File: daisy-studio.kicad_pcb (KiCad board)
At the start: 4 copper layers, 270 x 65 mm, 101 parts, among them J1 Power, J10 Earth, J2 GPIO Header, J3 Micro_SD_Card, J4 NCJ6FA-H-0, J5 NCJ6FA-H-0, J6 Conn_01x04_Pin, J7 Earth, J8 NCJ6FA-H-0, J9 NCJ6FA-H-0, Q1 SI2301CDS-T1-GE3, U1 TMA-1212D, U2 TPS54302, U3 Daisy_Seed, U4 H11L1SM, U5 THAT1246, U6 THAT1246, U7 THAT1646, U8 THAT1646

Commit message: lots of pcb work
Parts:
- removed the C11 at (68.6, 119.5)
- removed the D5 at (132.2, 118.9)
- removed the H3 at (199.2, 112.3)
- removed the H3 at (59.6, 77.8)
- removed the J7 at (119.1, 82.4)
- removed J_DC1: Barrel_Jack_2.1mm, Connector_BarrelJack:BarrelJack_Horizontal
- removed J_IN_ST1, J_OUT_ST1: STX-3100-3CB, Connector_Audio:Jack_3.5mm_Kycon_STX-3100-3CB
- removed J_MIDI_IN_1, J_MIDI_OUT_1, J_MIDI_THRU1: SDS-50J, daisy-studio:SDS50J
- removed the R23 at (115.0, 117.3)
- removed S1: LC2255EESP, daisy-studio:LC2255EESP
- removed the U1 at (316.8, 108.5)
- added C28: 1n, Capacitor_SMD:C_0805_2012Metric, F.Cu at (115.0, 70.1)
- added C29: 1n, Capacitor_SMD:C_0805_2012Metric, F.Cu at (120.0, 65.4)
- added C30: 100n, Capacitor_SMD:C_0805_2012Metric, F.Cu at (153.6, 51.1)
- added C31: 100n, Capacitor_SMD:C_0805_2012Metric, F.Cu at (122.0, 65.4)
- added C32: 10u, Capacitor_SMD:C_0805_2012Metric, F.Cu at (140.4, 54.5)
- added C33: 10u, Capacitor_SMD:C_0805_2012Metric, F.Cu at (131.4, 59.9)
- added C34: 100n, Capacitor_SMD:C_0805_2012Metric, F.Cu at (142.4, 54.5)
- added C35: 100n, Capacitor_SMD:C_0805_2012Metric, F.Cu at (134.8, 59.9)
- added C36: 10u, Capacitor_SMD:C_0805_2012Metric, F.Cu at (122.8, 54.5)
- added C37: 10u, Capacitor_SMD:C_0805_2012Metric, F.Cu at (113.8, 59.9)
- added C38: 100n, Capacitor_SMD:C_0805_2012Metric, F.Cu at (124.8, 54.5)
- added C39: 100n, Capacitor_SMD:C_0805_2012Metric, F.Cu at (117.2, 59.9)
- added C40: 47u, Capacitor_SMD:C_1206_3216Metric, F.Cu at (156.3, 62.2)
- added C41: 47u, Capacitor_SMD:C_1206_3216Metric, F.Cu at (164.2, 59.8)
- added C42: 47u, Capacitor_SMD:C_1206_3216Metric, F.Cu at (156.3, 69.7)
- added C43: 47u, Capacitor_SMD:C_1206_3216Metric, F.Cu at (164.2, 67.5)
- added C9: 1n C0G, Capacitor_SMD:C_0603_1608Metric, F.Cu at (183.5, 63.4)
- added D13: SM4004, Diode_SMD:D_MELF, F.Cu at (61.5, 54.6)
- added D14: LED, LED_THT:LED_D3.0mm, F.Cu at (105.4, 112.9)
- added D15: LED, LED_THT:LED_D3.0mm, F.Cu at (131.4, 112.9)
- added D2: SMBJ15CA, Diode_SMD:D_SMB, F.Cu at (262.8, 78.1)
- added H10: MountingHole, MountingHole:MountingHole_3.2mm_M3, F.Cu at (90.2, 112.9)
- added H11: MountingHole, MountingHole:MountingHole_3.2mm_M3, F.Cu at (149.9, 112.9)
- added H3: MountingHole_Pad, MountingHole:MountingHole_3.2mm_M3_Pad_Via, F.Cu at (149.9, 30.4)
- added H6: MountingHole, MountingHole:MountingHole_3.2mm_M3, F.Cu at (79.6, 96.0)
- added H7: MountingHole, MountingHole:MountingHole_3.2mm_M3, F.Cu at (259.2, 97.8)
- added H8: MountingHole, MountingHole:MountingHole_3.2mm_M3, F.Cu at (256.5, 30.4)
- added H9: MountingHole, MountingHole:MountingHole_3.2mm_M3, F.Cu at (30.4, 112.9)
- added J13: Conn_02x10_Odd_Even, Connector_IDC:IDC-Header_2x10_P2.54mm_Vertical, F.Cu at (101.8, 55.9)
- added J14: Conn_02x10_Odd_Even, Connector_IDC:IDC-Header_2x10_P2.54mm_Vertical, F.Cu at (101.8, 138.4)
- added J2: Conn_02x04_Odd_Even, Connector_PinHeader_2.54mm:PinHeader_2x04_P2.54mm_Vertical, F.Cu at (158.3, 54.8)
- added J3: Conn_02x04_Odd_Even, Connector_PinHeader_2.54mm:PinHeader_2x04_P2.54mm_Vertical, F.Cu at (172.6, 52.6)
- added J5: SDS-50J, daisy-studio:SDS50J, F.Cu at (203.2, 37.9)
- added PS1: RS3-1212D, daisy-studio:TMR1210, F.Cu at (247.6, 86.5)
- added Q2: MMBT3904, Package_TO_SOT_SMD:SOT-23, F.Cu at (131.7, 65.8)
- added Q3: MMBT3904, Package_TO_SOT_SMD:SOT-23, F.Cu at (139.3, 69.3)
- added Q4: MMBT3906, Package_TO_SOT_SMD:SOT-23, F.Cu at (131.7, 69.3)
- added Q5: MMBT3906, Package_TO_SOT_SMD:SOT-23, F.Cu at (139.2, 65.8)
- added R19: 2k2 1%, Resistor_SMD:R_0805_2012Metric, F.Cu at (89.2, 72.1)
- added R27: 3.3k 1%, Resistor_SMD:R_0805_2012Metric, F.Cu at (123.7, 69.1)
- added R28: 3.3k 1%, Resistor_SMD:R_0805_2012Metric, F.Cu at (123.7, 71.0)
- added R29: 1k, Resistor_SMD:R_0805_2012Metric, F.Cu at (88.5, 50.3)
- added R30: 1k, Resistor_SMD:R_0805_2012Metric, F.Cu at (90.6, 50.3)
- added R31: 10k 1%, Resistor_SMD:R_0805_2012Metric, F.Cu at (158.6, 59.2)
- added R32: 1.5k 1%, Resistor_SMD:R_0805_2012Metric, F.Cu at (158.6, 62.9)
- added R33: 1.5k 1%, Resistor_SMD:R_0805_2012Metric, F.Cu at (166.6, 59.2)
- added R34: 10k 1%, Resistor_SMD:R_0805_2012Metric, F.Cu at (166.6, 62.7)
- added R35: 10k 1%, Resistor_SMD:R_0805_2012Metric, F.Cu at (158.6, 66.7)
- added R36: 1.5k 1%, Resistor_SMD:R_0805_2012Metric, F.Cu at (158.6, 70.3)
- added R37: 1.5k 1%, Resistor_SMD:R_0805_2012Metric, F.Cu at (166.6, 66.9)
- added R38: 10k 1%, Resistor_SMD:R_0805_2012Metric, F.Cu at (166.6, 70.4)
- added RV1: 10k, Potentiometer_THT:Potentiometer_Bourns_3296W_Vertical, F.Cu at (77.5, 65.0)
- added RV2: 10k, Potentiometer_THT:Potentiometer_Bourns_3296W_Vertical, F.Cu at (104.5, 65.1)
- added RV3: 10k, Potentiometer_THT:Potentiometer_Bourns_3296W_Vertical, F.Cu at (152.2, 68.9)
- added RV4: 10k, Potentiometer_THT:Potentiometer_Bourns_3296W_Vertical, F.Cu at (146.7, 68.9)
- added RV5: 10k log, Potentiometer_THT:Potentiometer_Alpha_RD901F-40-00D_Single_Vertical_CircularHoles, F.Cu at (104.2, 131.4)
- added RV6: 10k log, Potentiometer_THT:Potentiometer_Alpha_RD901F-40-00D_Single_Vertical_CircularHoles, F.Cu at (44.7, 131.4)
- added RV7: 10k log, Potentiometer_THT:Potentiometer_Alpha_RD901F-40-00D_Single_Vertical_CircularHoles, F.Cu at (130.2, 131.4)
- added RV8: 10k log, Potentiometer_THT:Potentiometer_Alpha_RD901F-40-00D_Single_Vertical_CircularHoles, F.Cu at (71.2, 131.4)
- added SW1: Power, Connector_JST:JST_VH_B2P-VH_1x02_P3.96mm_Vertical, F.Cu at (254.6, 39.1)
- added U10: THAT1246, Package_SO:SOIC-8_3.9x4.9mm_P1.27mm, F.Cu at (135.5, 56.0)
- added U4: OPA1656ID, Package_SO:SOIC-8_3.9x4.9mm_P1.27mm, F.Cu at (91.0, 67.5)
- added U5: THAT1646, Package_SO:SOIC-8_3.9x4.9mm_P1.27mm, F.Cu at (46.7, 64.7)
- C10: value 10u -> 1n C0G; footprint Capacitor_SMD:C_0805_2012Metric -> Capacitor_SMD:C_0603_1608Metric
- C12, C14, C26: value 10u -> 100n
- C13, C15: value 100n -> 1n
- C16, C17: value 10u -> 100p C0G
- C4: value 100u/25V -> 100u 25V
- C6, C7: value 22u -> 22u 25V; footprint Capacitor_SMD:C_0805_2012Metric -> Capacitor_SMD:C_1206_3216Metric
- C8: value 75pf -> 75pF
- D1: value SMBJ15A -> SMBJ15CA
- D10, D11, D12, D6, D7, D8, D9: footprint Diode_SMD:D_SMA -> Diode_SMD:D_MELF
- D3: value BAT54S -> SMBJ15CA; footprint Package_TO_SOT_SMD:SOT-23 -> Diode_SMD:D_SMB
- D4: value BAT54S -> SMAJ5.0A; footprint Package_TO_SOT_SMD:SOT-23 -> Diode_SMD:D_SMA
- D5: renamed from D2; value 1N4148W -> 1N4148WS; footprint Diode_SMD:D_SOD-123 -> Diode_SMD:D_SOD-323
- H1, H2: value MountingHole -> MountingHole_Pad; footprint MountingHole:MountingHole_3.2mm_M3 -> MountingHole:MountingHole_3.2mm_M3_Pad_Via
- J1: value Power -> Barrel_Jack_MountingPin; footprint Connector_PinHeader_2.54mm:PinHeader_2x04_P2.54mm_Vertical -> Connector_BarrelJack:BarrelJack_Horizontal
- J10: value Earth -> NCJ6FA-H-0; footprint MountingHole:MountingHole_3.2mm_M3_Pad_Via -> Connector_Audio:Jack_XLR-6.35mm_Neutrik_NCJ6FA-H-0_Horizontal
- J6: value Conn_01x04_Pin -> SDS-50J; footprint Connector_PinHeader_2.54mm:PinHeader_1x04_P2.54mm_Vertical -> daisy-studio:SDS50J
- J7: renamed from J2; value GPIO Header -> Conn_02x12_Odd_Even
- J8: value NCJ6FA-H-0 -> SDS-50J; footprint Connector_Audio:Jack_XLR-6.35mm_Neutrik_NCJ6FA-H-0_Horizontal -> daisy-studio:SDS50J
- JP1: value Earth-Gnd Disconnect -> SolderJumper_2_Bridged
- Q1: footprint Package_TO_SOT_SMD:SOT-23 -> daisy-studio:SOT95P237X112-3N
- R10, R11, R7, R8, R9: value 47K -> 47k
- R20: value 1.2k -> 2k2 1%; footprint Resistor_SMD:R_0603_1608Metric -> Resistor_SMD:R_0805_2012Metric
- R21, R22: value 100k -> 15k; footprint Resistor_SMD:R_0603_1608Metric -> Resistor_SMD:R_0805_2012Metric
- R23: renamed from R19; value 1.2k -> 10k; footprint Resistor_SMD:R_0603_1608Metric -> Resistor_SMD:R_0805_2012Metric
- R24: value 100k -> 10k; footprint Resistor_SMD:R_0603_1608Metric -> Resistor_SMD:R_0805_2012Metric
- R25, R26: value 120R -> 12k 1%; footprint Resistor_SMD:R_0603_1608Metric -> Resistor_SMD:R_0805_2012Metric
- R3: value 13.7k -> 13.7k 1%
- R4: value 49.9R -> 49.9R 1%
- R6: value 13.3k 1% -> 13.3K 1%
- U2: renamed from U3; footprint daisy-studio:DAISY_SEED_SMT -> daisy-studio:DAISY_SEED
- U3: renamed from U4; value H11L1SM -> H11L1
- U6: value THAT1246 -> THAT1646
- U7: value THAT1646 -> OPA1656ID
- U8: value THAT1646 -> LM2903
- moved H5 288.4 mm to (31.1, 97.6)
- moved D3 186.5 mm to (261.8, 70.1), turned to 0 degrees
- moved D4 150.0 mm to (253.2, 69.0), turned to 0 degrees
- moved H4 139.8 mm to (185.3, 96.9)
- moved C21 131.0 mm to (46.9, 69.1), turned to 0 degrees
- moved C10 128.7 mm to (183.5, 66.0), turned to 0 degrees
- moved J9 126.5 mm to (40.2, 44.0)
- moved C20 125.8 mm to (50.2, 69.1), turned to 0 degrees
- moved C25 125.8 mm to (64.8, 69.1), turned to 0 degrees
- moved C24 124.6 mm to (68.3, 69.1), turned to 0 degrees
- moved D10 118.3 mm to (43.4, 58.1)
- moved C23 117.0 mm to (69.8, 63.0), turned to -90 degrees
- moved J1 114.9 mm to (246.8, 39.0)
- moved D6 113.9 mm to (50.5, 58.1), turned to 0 degrees
- moved D11 113.7 mm to (43.4, 54.6), turned to 0 degrees
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- renumbered C9 to C11, J4 to J11, J5 to J12, J3 to J4, U2 to U1, U5 to U9
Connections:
- C10 pad 1: +12VA -> AUDIO_IN_L
- C12 pad 1: GND -> -12VA
- C12 pad 2: -12VA -> GND
- C13 pad 1: GND -> -12VA
- C13 pad 2: -12VA -> GND
- C16 pad 1: GND -> Net-(U4A--)
- C16 pad 2: -12VA -> OUT_OPA_L
- C17 pad 1: Net-(S1-NO_1) -> Net-(U4B--)
- C17 pad 2: AUDIO_IN_L -> OUT_OPA_R
- C18 pad 1: Net-(S1-NO_2) -> +12VA
- C18 pad 2: AUDIO_IN_R -> GND
- C19 pad 2: -12VA -> +12VA
- C20 pad 1: +12VA -> -12VA
- C21 pad 1: +12VA -> GND
- C21 pad 2: GND -> -12VA
- C22 pad 1: GND -> +12VA
- C22 pad 2: -12VA -> GND
- C23 pad 2: -12VA -> +12VA
- C24 pad 1: +12VA -> -12VA
- C25 pad 1: +12VA -> GND
- C25 pad 2: GND -> -12VA
- C26 pad 1: GND -> -12VA
- C26 pad 2: -12VA -> GND
- C27 pad 1: GND -> -12VA
- C27 pad 2: -12VA -> GND
- D1 pad 2: GND -> Net-(D1-A2)
- D10 pad 1: Net-(D10-K) -> +12VA
- D10 pad 2: -12VA -> Net-(D10-A)
- D11 pad 1: Net-(D11-K) -> Net-(D10-A)
- D12 pad 1: Net-(D12-K) -> +12VA
- D12 pad 2: -12VA -> Net-(D12-A)
- D3 pad 1: GND -> +12VA
- D3 pad 2: +5V -> GND
- D4 pad 1: GND -> +5V
- D4 pad 2: +5V -> GND
- D6 pad 2: Net-(D10-K) -> Net-(D6-A)
- D7 pad 1: +12VA -> Net-(D6-A)
- D7 pad 2: Net-(D11-K) -> -12VA
- D8 pad 2: Net-(D12-K) -> Net-(D8-A)
- D9 pad 1: Net-(D5-A) (its old number) -> Net-(D8-A)
- J1 pad 1: +5V -> /Power/+12V_IN
- J1 pad 2: +12VA -> Net-(D1-A2)
- J1 pad 3: GND -> (no net)
- J10 pad 1: Earth -> CHASSIS
- J11 pad 1: Earth -> CHASSIS
- J11 pad G: Earth -> CHASSIS
- J11 pad S: Earth -> CHASSIS
- J12 pad 1: Earth -> CHASSIS
- J12 pad 2: Net-(U6-In+) -> Net-(U10A-+)
- J12 pad 3: Net-(U6-In-) -> Net-(U10A--)
- J12 pad G: Earth -> CHASSIS
- J12 pad R: Net-(U6-In-) -> Net-(U10A--)
- J12 pad S: Earth -> CHASSIS
- J12 pad T: Net-(U6-In+) -> Net-(U10A-+)
- J4 pad 10: GND -> (no net)
- J4 pad 11: GND -> (no net)
- J6 pad 1: AUDIO_IN_L -> unconnected-(J6-Pad1)
- J6 pad 2: AUDIO_IN_R -> GND
- J6 pad 3: AUDIO_OUT_L -> unconnected-(J6-Pad3)
- J6 pad 4: AUDIO_OUT_R -> Net-(J6-Pad4)
- J8 pad 1: Earth -> unconnected-(J8-Pad1)
- J8 pad 2: Net-(D5-A) (its old number) -> GND
- J8 pad 3: Net-(D11-K) -> unconnected-(J8-Pad3)
- J9 pad 1: Earth -> CHASSIS
- J9 pad 2: Net-(D10-K) -> Net-(D6-A)
- J9 pad 3: Net-(D12-K) -> Net-(D10-A)
- J9 pad G: Earth -> CHASSIS
- J9 pad R: Net-(D12-K) -> Net-(D10-A)
- J9 pad S: Earth -> CHASSIS
- J9 pad T: Net-(D10-K) -> Net-(D6-A)
- JP1 pad 2: Earth -> CHASSIS
- Q1 pad 2: /Power/+12V_IN -> Net-(Q1-S)
- R1 pad 2: GND -> Net-(D1-A2)
- R12 pad 2: Net-(J_MIDI_OUT_1-Pad4) -> Net-(J6-Pad4)
- R13 pad 1: Net-(J_MIDI_OUT_1-Pad5) -> Net-(J6-Pad5)
- R17 pad 2: Net-(J_MIDI_THRU1-Pad4) -> Net-(J8-Pad4)
- R18 pad 2: Net-(J_MIDI_THRU1-Pad5) -> Net-(J8-Pad5)
- R20 pad 1: Net-(J_IN_ST1-R) -> Net-(U4B--)
- R20 pad 2: Net-(S1-NO_2) -> AUDIO_OUT_R
- R21 pad 1: AUDIO_IN_L -> Net-(R21-Pad1)
- R21 pad 2: +5V -> Net-(U4A--)
- R22 pad 1: GND -> Net-(R22-Pad1)
- R22 pad 2: AUDIO_IN_L -> Net-(U4B--)
- R23 pad 1: Net-(J_IN_ST1-T) -> Net-(R23-Pad1)
- R23 pad 2: Net-(S1-NO_1) -> Net-(U7A--)
- R24 pad 1: GND -> Net-(R24-Pad1)
- R24 pad 2: AUDIO_IN_R -> Net-(U10A-S)
- R25 pad 1: Net-(S1-COM_2) -> Net-(U7A--)
- R25 pad 2: GND -> IN_OPA_L
- R26 pad 1: Net-(S1-COM_1) -> Net-(U10A-S)
- R26 pad 2: GND -> IN_OPA_R
- U6 pad 1: GND -> Net-(D12-A)
- U6 pad 2: Net-(U6-In-) -> Net-(D12-A)
- U6 pad 3: Net-(U6-In+) -> GND
- U6 pad 4: -12VA -> OUT_WIPER_R
- U6 pad 5: Net-(J_IN_ST1-R) -> -12VA
- U6 pad 6: Net-(J_IN_ST1-R) -> +12VA
- U6 pad 7: +12VA -> Net-(D8-A)
- U6 pad 8: unconnected-(U6-NC-Pad8) -> Net-(D8-A)
- U7 pad 1: Net-(D5-A) (its old number) -> IN_OPA_L
- U7 pad 2: unconnected-(U7-Sense--Pad2) -> Net-(U7A--)
- U7 pad 4: AUDIO_OUT_L -> -12VA
- U7 pad 5: -12VA -> GND
- U7 pad 6: +12VA -> Net-(U10A-S)
- U7 pad 7: unconnected-(U7-Sense+-Pad7) -> IN_OPA_R
- U7 pad 8: Net-(D11-K) -> +12VA
- U8 pad 1: Net-(D10-K) -> CLIP_LED_K_L
- U8 pad 2: unconnected-(U8-Sense--Pad2) -> AUDIO_IN_L
- U8 pad 3: GND -> /Audio Input/IN_THRESH_L
- U8 pad 4: AUDIO_OUT_R -> -12VA
- U8 pad 5: -12VA -> /Audio Input/IN_THRESH_R
- U8 pad 6: +12VA -> AUDIO_IN_R
- U8 pad 7: unconnected-(U8-Sense+-Pad7) -> CLIP_LED_K_R
- U8 pad 8: Net-(D12-K) -> +12VA
- U9 pad 5: Net-(J_IN_ST1-T) -> Net-(U7A--)
- U9 pad 6: Net-(J_IN_ST1-T) -> Net-(R23-Pad1)
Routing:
- net +12VA: track 429.8 -> 32.9 mm, vias 13 -> 1
- net -12VA: track 404.0 -> 30.6 mm, vias 12 -> 2
- net +5V: track 312.3 -> 0.00 mm, vias 8 -> 0
- net +3V3D: track 198.3 -> 0.00 mm, vias 6 -> 0
- net Net-(J_IN_ST1-T): track 162.6 -> 0.00 mm, vias 1 -> 0
- net AUDIO_IN_L: track 184.2 -> 34.3 mm
- net CLIP_LED_K_R: track 0.00 -> 146.1 mm, vias 0 -> 3
- net Net-(J_IN_ST1-R): track 143.5 -> 0.00 mm, vias 1 -> 0
- net Net-(S1-NO_1): track 126.1 -> 0.00 mm, vias 2 -> 0
- net Net-(S1-NO_2): track 122.8 -> 0.00 mm
- net OUT_WIPER_L: track 0.00 -> 107.2 mm, vias 0 -> 1
- net +3V3A: track 105.5 -> 0.00 mm, vias 1 -> 0
- net CLIP_LED_K_L: track 0.00 -> 104.3 mm, vias 0 -> 1
- net AUDIO_IN_R: track 145.2 -> 42.4 mm, vias 2 -> 0
- net GPIO_D15: track 101.8 -> 0.00 mm
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- added copper zone on B.Cu, net CHASSIS
- added copper zone on In1.Cu, net CHASSIS
- removed copper zone on B.Cu, net Earth
- removed copper zone on In1.Cu, net Earth
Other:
- board size 270 x 65 mm -> 236.7 x 119.3 mm

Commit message: lots of pcb work
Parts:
- J2: value Conn_02x04_Odd_Even -> ~; footprint Connector_PinHeader_2.54mm:PinHeader_2x04_P2.54mm_Vertical -> Connector_PinHeader_2.54mm:PinHeader_2x03_P2.54mm_Vertical
- J4: value Micro_SD_Card -> Micro_SD_Card_Det2; footprint Connector_Card:microSD_HC_Hirose_DM3AT-SF-PEJM5 -> Connector_Card:microSD_HC_Hirose_DM3BT-DSF-PEJS; moved to B.Cu
- J7: footprint Connector_PinHeader_2.54mm:PinHeader_2x12_P2.54mm_Vertical_SMD -> Connector_PinHeader_2.54mm:PinHeader_2x14_P2.54mm_Vertical_SMD
- U2: footprint daisy-studio:DAISY_SEED -> daisy-studio:DAISY_SEED_SMT
- U3: footprint Package_SO:SO-6_4.4x3.6mm_P1.27mm -> Package_DIP:SMDIP-6_W7.62mm
- moved J3 131.2 mm to (302.9, 68.2), turned to 180 degrees
- moved C1 62.5 mm to (302.1, 86.5)
- moved C2 62.5 mm to (302.1, 89.5)
- moved L1 62.5 mm to (306.3, 86.2)
- moved L2 62.5 mm to (302.8, 86.5)
- moved H7 58.0 mm to (312.8, 75.5)
- moved J1 56.3 mm to (303.1, 39.0)
- moved H8 55.3 mm to (311.8, 30.4)
- moved J7 53.8 mm to (231.2, 50.1), turned to 0 degrees
- moved PS1 50.5 mm to (297.2, 77.3)
- moved C4 49.3 mm to (305.5, 50.7)
- moved C5 49.3 mm to (287.9, 60.7)
- moved C6 49.3 mm to (294.5, 69.0)
- moved C7 49.3 mm to (294.5, 67.0)
- moved C8 49.3 mm to (293.7, 60.4)
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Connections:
- J2 pad 6: (no net) -> GND
- J4 pad 10: (no net) -> unconnected-(J4-DET_A-Pad10)
- J4 pad 11: (no net) -> GND
- J4 pad 9: GND -> unconnected-(J4-DET_B-Pad9)
- J7 pad 1: GPIO_D0 -> unconnected-(J7-Pin_1-Pad1)
- J7 pad 10: GPIO_D19 -> unconnected-(J7-Pin_10-Pad10)
- J7 pad 11: GPIO_D11 -> GPIO_D8
- J7 pad 12: GPIO_D20 -> unconnected-(J7-Pin_12-Pad12)
- J7 pad 13: GPIO_D12 -> GPIO_D7
- J7 pad 14: GPIO_D21 -> unconnected-(J7-Pin_14-Pad14)
- J7 pad 15: GPIO_D29 -> unconnected-(J7-Pin_15-Pad15)
- J7 pad 16: GPIO_D22 -> unconnected-(J7-Pin_16-Pad16)
- J7 pad 17: GPIO_D30 -> unconnected-(J7-Pin_17-Pad17)
- J7 pad 18: GPIO_D23 -> unconnected-(J7-Pin_18-Pad18)
- J7 pad 19: GPIO_D28 -> unconnected-(J7-Pin_19-Pad19)
- J7 pad 2: GPIO_D15 -> unconnected-(J7-Pin_2-Pad2)
- J7 pad 20: GPIO_D24 -> unconnected-(J7-Pin_20-Pad20)
- J7 pad 21: GPIO_D27 -> unconnected-(J7-Pin_21-Pad21)
- J7 pad 22: GPIO_D25 -> unconnected-(J7-Pin_22-Pad22)
- J7 pad 23: GPIO_D26 -> unconnected-(J7-Pin_23-Pad23)
- J7 pad 24: GND -> unconnected-(J7-Pin_24-Pad24)
- J7 pad 3: GPIO_D7 -> GPIO_D12
- J7 pad 4: GPIO_D16 -> unconnected-(J7-Pin_4-Pad4)
- J7 pad 5: GPIO_D8 -> GPIO_D11
- J7 pad 6: GPIO_D17 -> unconnected-(J7-Pin_6-Pad6)
- J7 pad 7: GPIO_D9 -> GPIO_D10
- J7 pad 8: GPIO_D18 -> unconnected-(J7-Pin_8-Pad8)
- J7 pad 9: GPIO_D10 -> GPIO_D9
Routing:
- net AUDIO_OUT_L: track 0.00 -> 93.1 mm
- net AUDIO_OUT_R: track 0.00 -> 90.7 mm
- net GPIO_D12: track 0.00 -> 55.1 mm, vias 0 -> 2
- net GPIO_D11: track 0.00 -> 53.7 mm, vias 0 -> 2
- net GPIO_D10: track 0.00 -> 46.0 mm, vias 0 -> 2
- net MIDI_RX: track 0.00 -> 43.4 mm, vias 0 -> 3
- net GPIO_D9: track 0.00 -> 42.8 mm, vias 0 -> 2
- net SD_D0: track 0.00 -> 41.2 mm, vias 0 -> 2
- net SD_D1: track 0.00 -> 40.6 mm, vias 0 -> 2
- net GPIO_D8: track 0.00 -> 39.0 mm, vias 0 -> 2
- net SD_CMD: track 0.00 -> 38.9 mm, vias 0 -> 2
- net SD_CK: track 0.00 -> 36.8 mm, vias 0 -> 2
- net AUDIO_IN_L: track 34.3 -> 70.6 mm, vias 0 -> 2
- net GPIO_D7: track 0.00 -> 33.5 mm, vias 0 -> 2
- net SD_D2: track 0.00 -> 30.1 mm, vias 0 -> 2
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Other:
- board size 236.7 x 119.3 mm -> 251.3 x 119.3 mm

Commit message: lots of pcb work
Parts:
- moved D2 73.1 mm to (237.8, 79.9)
- moved D3 71.9 mm to (239.5, 73.7), turned to 90 degrees
- moved J3 64.4 mm to (239.3, 58.0), turned to 0 degrees
- moved L1 64.3 mm to (242.5, 78.4), turned to 90 degrees
- moved L2 61.5 mm to (242.5, 74.4), turned to -90 degrees
- moved C2 59.5 mm to (244.4, 74.7), turned to -90 degrees
- moved C1 58.2 mm to (244.4, 78.2), turned to 90 degrees
- moved H7 51.1 mm to (261.7, 77.5)
- moved H8 49.9 mm to (261.8, 30.4)
- moved PS1 46.4 mm to (251.5, 69.5), turned to -90 degrees
- moved J2 39.3 mm to (158.0, 78.0), turned to -90 degrees
- moved R29 20.7 mm to (73.0, 64.0), turned to -90 degrees
- moved R30 13.7 mm to (87.7, 63.6), turned to 0 degrees
- moved J7 7.73 mm to (230.4, 57.7)
- moved H6 7.66 mm to (90.0, 77.5)
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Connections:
- J7 pad 10: unconnected-(J7-Pin_10-Pad10) -> GPIO_D23
- J7 pad 12: unconnected-(J7-Pin_12-Pad12) -> GPIO_D24
- J7 pad 14: unconnected-(J7-Pin_14-Pad14) -> GPIO_D25
- J7 pad 15: unconnected-(J7-Pin_15-Pad15) -> GPIO_D15
- J7 pad 16: unconnected-(J7-Pin_16-Pad16) -> GPIO_D26
- J7 pad 17: unconnected-(J7-Pin_17-Pad17) -> GPIO_D16
- J7 pad 18: unconnected-(J7-Pin_18-Pad18) -> GPIO_D27
- J7 pad 19: unconnected-(J7-Pin_19-Pad19) -> GPIO_D17
- J7 pad 20: unconnected-(J7-Pin_20-Pad20) -> GPIO_D28
- J7 pad 21: unconnected-(J7-Pin_21-Pad21) -> GPIO_D18
- J7 pad 22: unconnected-(J7-Pin_22-Pad22) -> GPIO_D29
- J7 pad 23: unconnected-(J7-Pin_23-Pad23) -> GPIO_D19
- J7 pad 24: unconnected-(J7-Pin_24-Pad24) -> GPIO_D30
- J7 pad 25: unconnected-(J7-Pin_25-Pad25) -> GPIO_D20
- J7 pad 26: unconnected-(J7-Pin_26-Pad26) -> GND
- J7 pad 27: unconnected-(J7-Pin_27-Pad27) -> GND
- J7 pad 28: unconnected-(J7-Pin_28-Pad28) -> GND
- J7 pad 4: unconnected-(J7-Pin_4-Pad4) -> GPIO_D0
- J7 pad 6: unconnected-(J7-Pin_6-Pad6) -> GPIO_D21
- J7 pad 8: unconnected-(J7-Pin_8-Pad8) -> GPIO_D22
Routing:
- net -12VA: track 30.6 -> 395.8 mm, vias 2 -> 10
- net +12VA: track 32.9 -> 355.9 mm, vias 1 -> 14
- net +3V3D: track 4.85 -> 142.1 mm, vias 0 -> 5
- net GPIO_D16: track 0.00 -> 64.1 mm, vias 0 -> 2
- net GPIO_D15: track 0.00 -> 62.3 mm, vias 0 -> 2
- net GPIO_D21: track 0.00 -> 59.4 mm, vias 0 -> 2
- net GPIO_D22: track 0.00 -> 59.2 mm, vias 0 -> 2
- net GPIO_D18: track 0.00 -> 58.0 mm, vias 0 -> 2
- net GPIO_D17: track 0.00 -> 57.5 mm, vias 0 -> 2
- net GPIO_D20: track 0.00 -> 53.9 mm
- net GPIO_D24: track 0.00 -> 52.2 mm, vias 0 -> 2
- net GPIO_D19: track 0.00 -> 52.0 mm, vias 0 -> 2
- net GPIO_D23: track 0.00 -> 50.6 mm, vias 0 -> 2
- net GPIO_D26: track 0.00 -> 44.3 mm, vias 0 -> 2
- net GPIO_D25: track 0.00 -> 44.3 mm, vias 0 -> 2
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- added copper zone on B.Cu, net (none)
- added copper zone on In1.Cu, net (none)
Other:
- board size 251.3 x 119.3 mm -> 241.5 x 119.3 mm

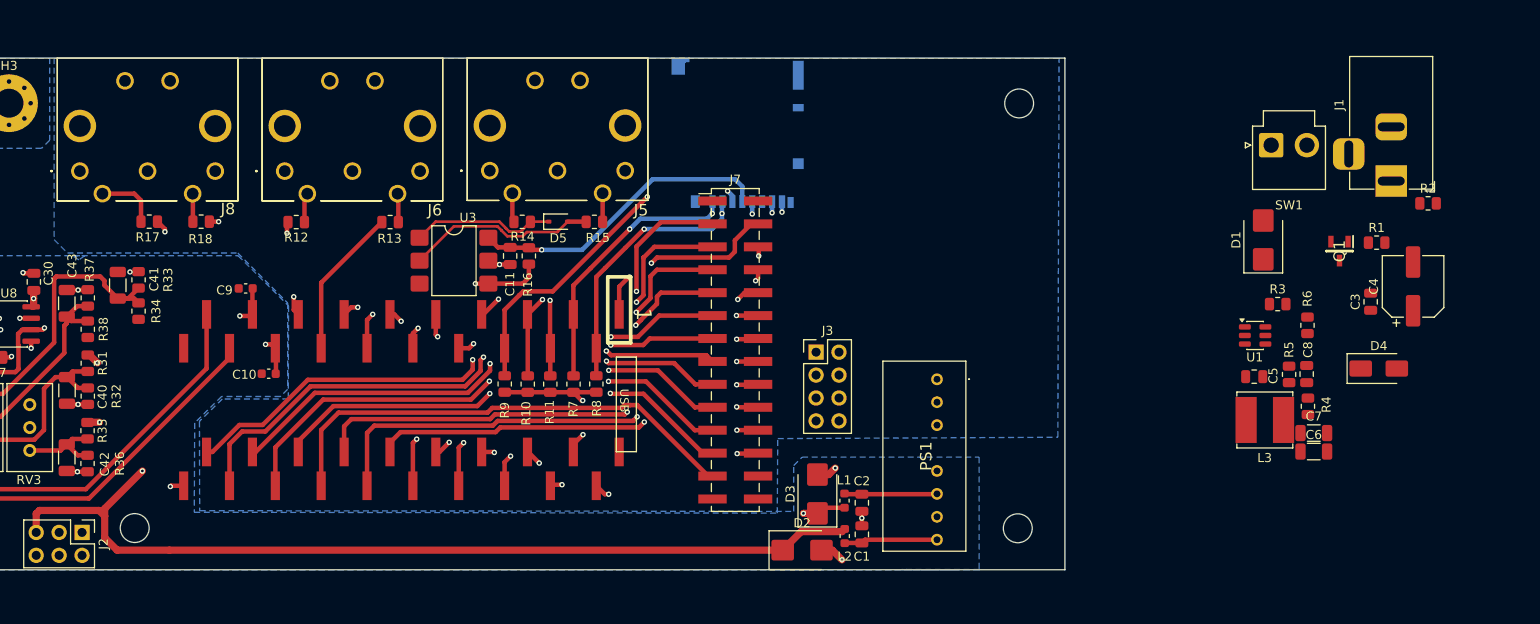
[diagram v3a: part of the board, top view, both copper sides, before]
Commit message: clean up some power cap issues
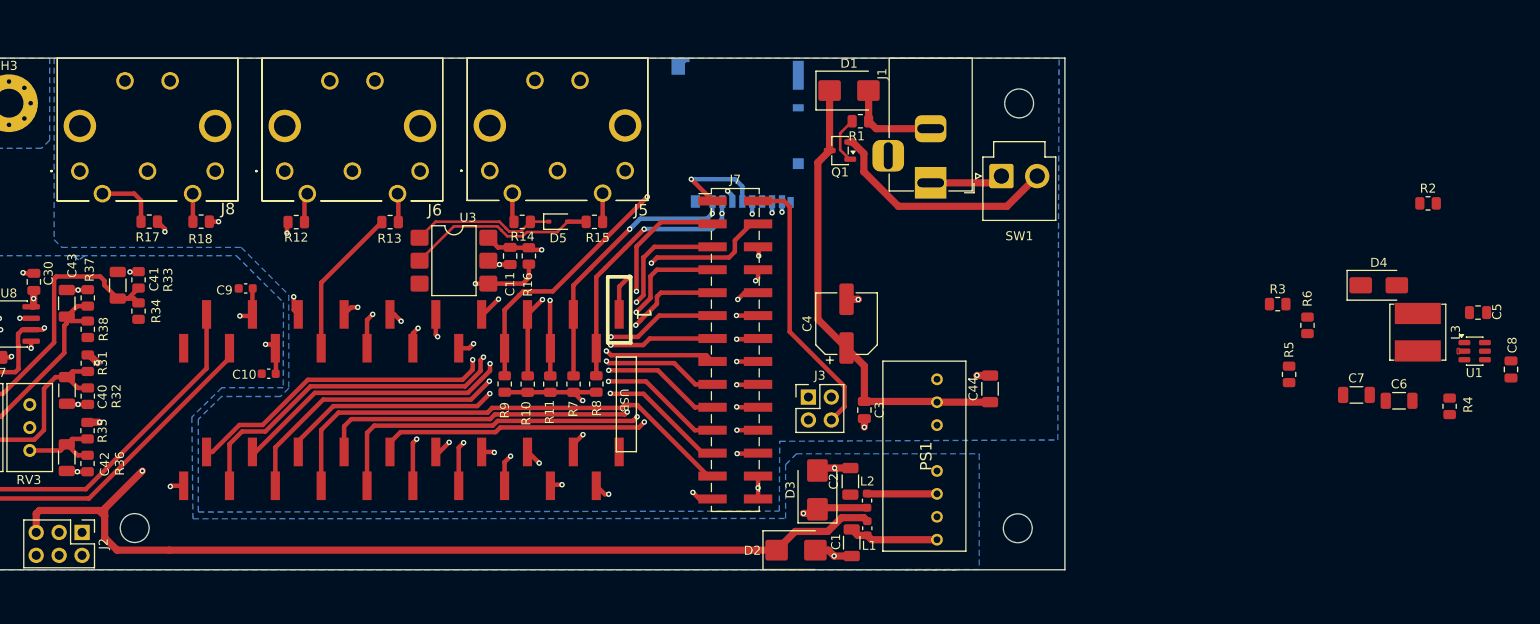
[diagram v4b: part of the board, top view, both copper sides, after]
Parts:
- added C44: 10u 25V, Capacitor_SMD:C_1206_3216Metric, F.Cu at (258.6, 62.0)
- C1, C2: value 10u -> 22u 25V; footprint Capacitor_SMD:C_0805_2012Metric -> Capacitor_SMD:C_1206_3216Metric
- J3: value Conn_02x04_Odd_Even -> Conn_02x02_Odd_Even; footprint Connector_PinHeader_2.54mm:PinHeader_2x04_P2.54mm_Vertical -> Connector_PinHeader_2.54mm:PinHeader_2x02_P2.54mm_Vertical
- Q1: value SI2301CDS-T1-GE3 -> DMP3056L-13; footprint daisy-studio:SOT95P237X112-3N -> Package_TO_SOT_SMD:SOT-23-3
- moved C4 62.9 mm to (242.7, 54.8)
- moved R1 58.8 mm to (244.2, 32.4)
- moved C3 57.4 mm to (244.7, 64.4), turned to -90 degrees
- moved Q1 56.5 mm to (242.0, 35.6), turned to 180 degrees
- moved J1 51.0 mm to (252.0, 39.2)
- moved D1 48.8 mm to (243.0, 29.0), turned to 0 degrees
- moved SW1 30.1 mm to (259.9, 38.5)
- moved C5 25.8 mm to (312.7, 53.6)
- moved U1 24.4 mm to (312.3, 57.9)
- moved C8 22.6 mm to (316.3, 59.9)
- moved L3 19.5 mm to (306.0, 55.8), turned to 90 degrees
- moved R4 15.7 mm to (309.5, 64.0)
- moved C6 11.0 mm to (303.9, 63.4)
- moved D4 9.22 mm to (301.7, 50.6)
- moved C7 6.34 mm to (299.2, 62.7)
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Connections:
- J7 pad 1: unconnected-(J7-Pin_1-Pad1) -> +3V3D
- J7 pad 2: unconnected-(J7-Pin_2-Pad2) -> +5V
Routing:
- net +12V_RAW: track 0.00 -> 51.1 mm
- net +5V: track 37.9 -> 65.7 mm
- net Net-(Q1-S): track 0.00 -> 26.3 mm
- net Net-(D1-A2): track 0.00 -> 11.5 mm
- net GND: track 58.5 -> 68.1 mm, vias 1213 -> 1217
- net /Power/+12V_IN: track 0.00 -> 8.15 mm
- net +3V3D: track 142.1 -> 148.8 mm, vias 5 -> 6
- net Net-(Q1-G): track 0.00 -> 5.17 mm
- net -12VA: track 395.8 -> 399.7 mm
- net +12VA: track 355.9 -> 359.3 mm
- net Net-(PS1-+VOUT): track 10.3 -> 7.82 mm
- added copper zone on F.Cu, net Net-(U1-SW)
- removed copper zone on B.Cu, net (none)
- removed copper zone on In1.Cu, net (none)

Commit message: final layout
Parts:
- moved C38 66.4 mm to (250.7, 49.5)
- moved C37 61.0 mm to (251.7, 52.3), turned to 0 degrees
- moved U10 59.0 mm to (253.9, 49.6), turned to 180 degrees
- moved R36 58.2 mm to (251.9, 55.7), turned to 180 degrees
- moved R34 53.4 mm to (254.0, 46.9), turned to 180 degrees
- moved C40 47.7 mm to (257.1, 54.2), turned to 90 degrees
- moved R38 47.4 mm to (246.6, 51.4), turned to -90 degrees
- moved C41 45.2 mm to (254.8, 54.2), turned to 90 degrees
- moved L1 44.7 mm to (261.5, 51.7), turned to -90 degrees
- moved R35 44.0 mm to (248.5, 52.6)
- moved D15 40.6 mm to (261.8, 58.1)
- moved R37 39.1 mm to (252.2, 44.9), turned to 180 degrees
- moved C39 12.5 mm to (257.1, 49.6), turned to -90 degrees
- moved C36 2.76 mm to (241.0, 52.7)
- moved C44 0.18 mm to (243.1, 79.1)
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- renumbered C19 to C1, C12 to C10, C24 to C11, C37 to C12, C14 to C13, C26 to C14, C17 to C15, C15 to C16, C39 to C17, C36 to C18, C35 to C19, C21 to C2, C38 to C20, C33 to C21, C29 to C22, C31 to C23, C28 to C24, C34 to C25, C27 to C26, C41 to C27, C32 to C28, C40 to C29, C18 to C3, C43 to C30, C30 to C31, C42 to C32, C10 to C33, C9 to C34, C11 to C35, C4 to C36, C5 to C37, C8 to C38, C44 to C39, C20 to C4, C6 to C40, C7 to C41, C3 to C42, C2 to C43, C1 to C44, C23 to C5, C25 to C6, C22 to C7, C16 to C8, C13 to C9, D6 to D1, D15 to D10, D5 to D11, D3 to D12, D2 to D13, D1 to D14, D4 to D15, D10 to D2, D13 to D3, D11 to D4, D12 to D5, D7 to D6, D8 to D7, D9 to D8, D14 to D9, H8 to H10, H7 to H11, H5 to H2, H9 to H3, H2 to H4, H6 to H5, H10 to H6, H3 to H7, H4 to H8, H11 to H9, J9 to J1, J5 to J10, J7 to J11, J3 to J12, J1 to J13, J4 to J14, J10 to J2, J13 to J3, J11 to J4, J14 to J5, J12 to J6, J8 to J7, J2 to J8, J6 to J9, L3 to L1, L1 to L3, Q2 to Q1, Q4 to Q2, Q5 to Q3, Q3 to Q4, Q1 to Q5, R30 to R1, R27 to R10, R28 to R11, R37 to R12, R34 to R13, R33 to R14, R32 to R15, R24 to R16, R38 to R17, R31 to R18, R36 to R19, R21 to R2, R35 to R20, R12 to R21, R17 to R22, R18 to R23, R14 to R24, R9 to R25, R11 to R26, R7 to R27, R10 to R28, R13 to R29, R29 to R3, R16 to R30, R15 to R31, R8 to R32, R1 to R33, R2 to R34, R5 to R35, R4 to R36, R3 to R37, R6 to R38, R25 to R4, R19 to R5, R20 to R6, R22 to R7, R23 to R8, R26 to R9, RV6 to RV1, RV1 to RV2, RV8 to RV3, RV2 to RV4, RV7 to RV6, RV3 to RV7, RV4 to RV8, U5 to U1, U1 to U10, U6 to U2, U4 to U3, U9 to U4, U10 to U5, U7 to U6, U8 to U7, U3 to U8, U2 to U9
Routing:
- net +5V: track 65.7 -> 91.9 mm, vias 1 -> 8
- net +12V_RAW: track 51.1 -> 70.0 mm, vias 0 -> 1
- net Net-(U1-SW): track 0.00 -> 10.5 mm, vias 0 -> 3
- net GND: track 68.1 -> 77.9 mm, vias 1217 -> 1222
- net Net-(U1-FB): track 0.00 -> 8.47 mm
- net Net-(C8-Pad1): track 0.00 -> 7.81 mm
- net -12VA: track 399.7 -> 392.1 mm, vias 10 -> 9
- net Net-(U1-EN): track 0.00 -> 5.79 mm
- net Net-(D10-A): track 44.0 -> 40.9 mm
- net Net-(D6-A): track 59.7 -> 57.1 mm
- net Net-(U1-BOOT): track 0.00 -> 2.47 mm
- net GPIO_D19: track 52.0 -> 49.8 mm
- net +12VA: track 359.3 -> 357.1 mm
- net Net-(U9A--): track 16.5 -> 14.8 mm
- net +3V3D: track 148.8 -> 147.3 mm
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- added copper zone on In2.Cu, net +12V_RAW
- added copper zone on In2.Cu, net +5V
- added copper zone on In2.Cu, net Net-(U1-SW)
- removed copper zone on F.Cu, net Net-(U1-SW)
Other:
- board text added: "->"

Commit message: clean up vias
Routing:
- net GND: track 77.9 -> 229.6 mm, vias 1222 -> 2960
- net -12VA: track 392.1 -> 408.6 mm, vias 9 -> 12
- net Net-(U10-SW): track 10.5 -> 24.0 mm, vias 3 -> 12
- net Net-(D3-K): track 53.8 -> 56.9 mm
- net +12VA: track 357.1 -> 354.4 mm
- net OUT_OPA_R: track 67.9 -> 70.4 mm
- net Net-(PS1-+VOUT): track 7.74 -> 9.61 mm
- net CHASSIS: vias 0 -> 815

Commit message: Rev 2 Fab sent
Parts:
- removed H3, H9: MountingHole, MountingHole:MountingHole_3.2mm_M3
- moved RV6 108.9 mm to (38.6, 72.5), turned to 0 degrees
- moved J5 100.9 mm to (31.7, 65.8), turned to 180 degrees
- moved RV1 100.3 mm to (38.6, 31.4), turned to 0 degrees
- moved RV5 97.9 mm to (38.6, 58.8), turned to 0 degrees
- moved D10 93.5 mm to (54.2, 60.0), turned to -90 degrees
- moved RV3 92.2 mm to (38.6, 45.1), turned to 0 degrees
- moved D9 83.9 mm to (54.2, 46.3), turned to -90 degrees
- moved H6 67.4 mm to (57.1, 54.1), turned to -90 degrees
- moved C12 36.8 mm to (150.6, 59.8)
- moved C16 36.8 mm to (134.8, 64.7)
- moved C19 36.8 mm to (171.7, 59.8)
- moved C21 36.8 mm to (168.2, 59.8)
- moved C22 36.8 mm to (156.8, 65.3)
- moved C23 36.8 mm to (158.8, 65.3)
- moved C27 36.8 mm to (198.8, 50.5)
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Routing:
- net OUT_OPA_R: track 70.4 -> 44.6 mm
- net IN_WIPER_R: track 87.5 -> 62.4 mm
- net CLIP_LED_A_R: track 69.7 -> 45.5 mm
- net CLIP_LED_K_R: track 146.1 -> 123.3 mm, vias 3 -> 2
- net OUT_OPA_L: track 71.2 -> 51.9 mm
- net OUT_WIPER_L: track 107.2 -> 87.9 mm
- net IN_OPA_R: track 68.8 -> 53.0 mm
- net OUT_WIPER_R: track 65.6 -> 54.5 mm
- net CLIP_LED_K_L: track 104.3 -> 94.9 mm
- net IN_WIPER_L: track 48.3 -> 40.4 mm
- net IN_OPA_L: track 36.2 -> 28.9 mm
- net CLIP_LED_A_L: track 49.8 -> 44.5 mm
- net GND: vias 2960 -> 2242
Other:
- board size 241.5 x 119.3 mm -> 278.3 x 56.7 mm
- board text added: "Daisy Seed Rev 7 ONLY"
- board text added: "Gain/Clip Daisy-Studio Rev2 29 Apr 2026 Rasheed Abdul-Aziz"
- board text added: "Main Daisy-Studio Rev2 29 Apr 2026 Rasheed Abdul-Aziz"
- board text added: "V-Groove"
